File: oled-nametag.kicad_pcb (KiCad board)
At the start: 4 copper layers, 88 x 30 mm, 138 parts, among them J1 USB_C_Receptacle_USB2.0, J2 I2C, J3 LOAD, Q1 AO3401A, Q2 AO3401A, Q4 AO3400A, Q5 AO3400A, Q6 2N7002, SW1 Power, SW2 BTN1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

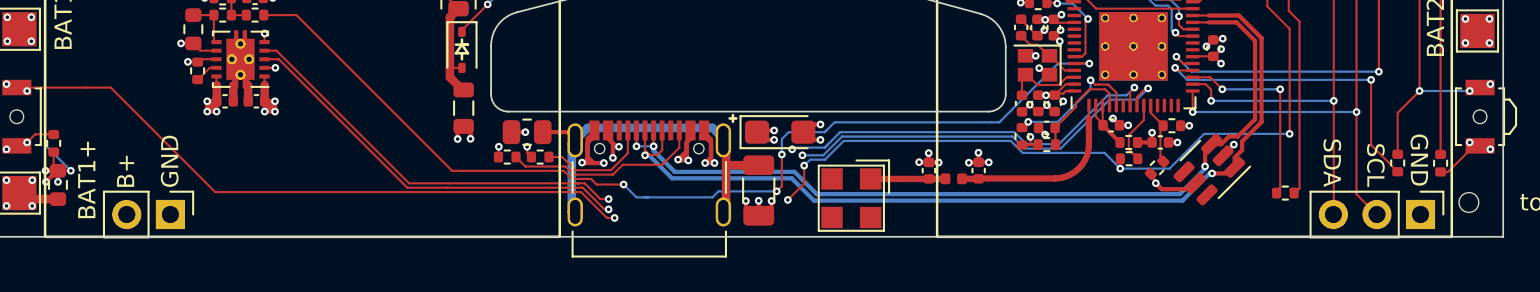
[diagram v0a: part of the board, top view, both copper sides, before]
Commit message: Unify text orientation
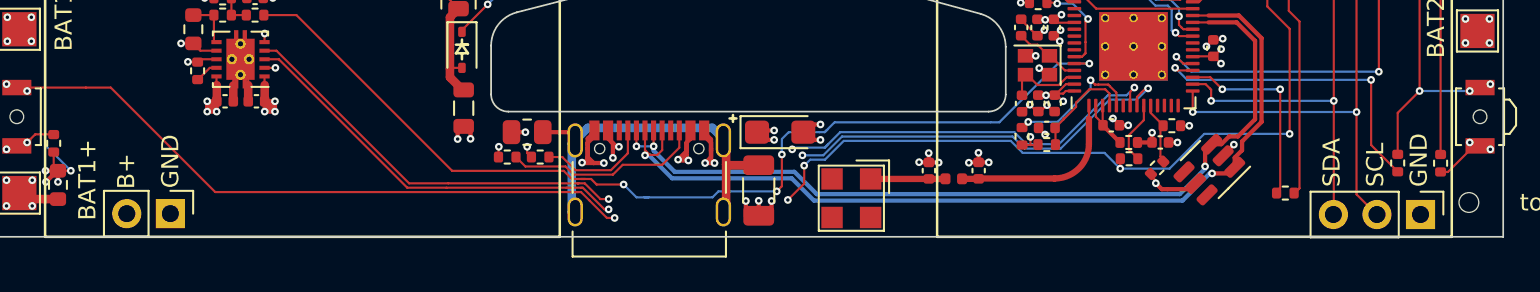
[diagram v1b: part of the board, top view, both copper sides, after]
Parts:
- moved J3 0.05 mm to (30.3, 48.6)
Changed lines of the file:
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@@
   )
   (footprint "Connector_PinHeader_2.54mm:PinHeader_1x02_P2.54mm_Vertical" (layer "F.Cu")
-    (at 30.3 48.7 -90)
+    (at 30.3 48.65 -90)
     (descr "Through hole straight pin header, 1x02, 2.54mm pitch, single row")
     (tags "Through hole pin header THT 1x02 2.54mm single row")
@@
     (effects (font (size 1 1) (thickness 0.15)) (justify left))
   )
-  (gr_text "GND" (at 103.079999 47.1 -90) (layer "F.SilkS")
-    (effects (font (size 1 1) (thickness 0.15)) (justify right))
+  (gr_text "GND" (at 103.079999 47.1 90) (layer "F.SilkS")
+    (effects (font (size 1 1) (thickness 0.15)) (justify left))
   )
-  (gr_text "SCL" (at 100.54 47.1 -90) (layer "F.SilkS")
-    (effects (font (size 1 1) (thickness 0.15)) (justify right))
+  (gr_text "SCL" (at 100.54 47.1 90) (layer "F.SilkS")
+    (effects (font (size 1 1) (thickness 0.15)) (justify left))
   )
   (gr_text "JLCJLCJLCJLC" (at 64 32.85) (layer "F.SilkS")
@@
     (effects (font (size 1 1) (thickness 0.15)) (justify left))
   )
-  (gr_text "SDA" (at 98 47.1 -90) (layer "F.SilkS")
-    (effects (font (size 1 1) (thickness 0.15)) (justify right))
+  (gr_text "SDA" (at 98 47.1 90) (layer "F.SilkS")
+    (effects (font (size 1 1) (thickness 0.15)) (justify left))
   )
   (gr_text "BAT1+" (at 24.88 46.68 90) (layer "F.SilkS")

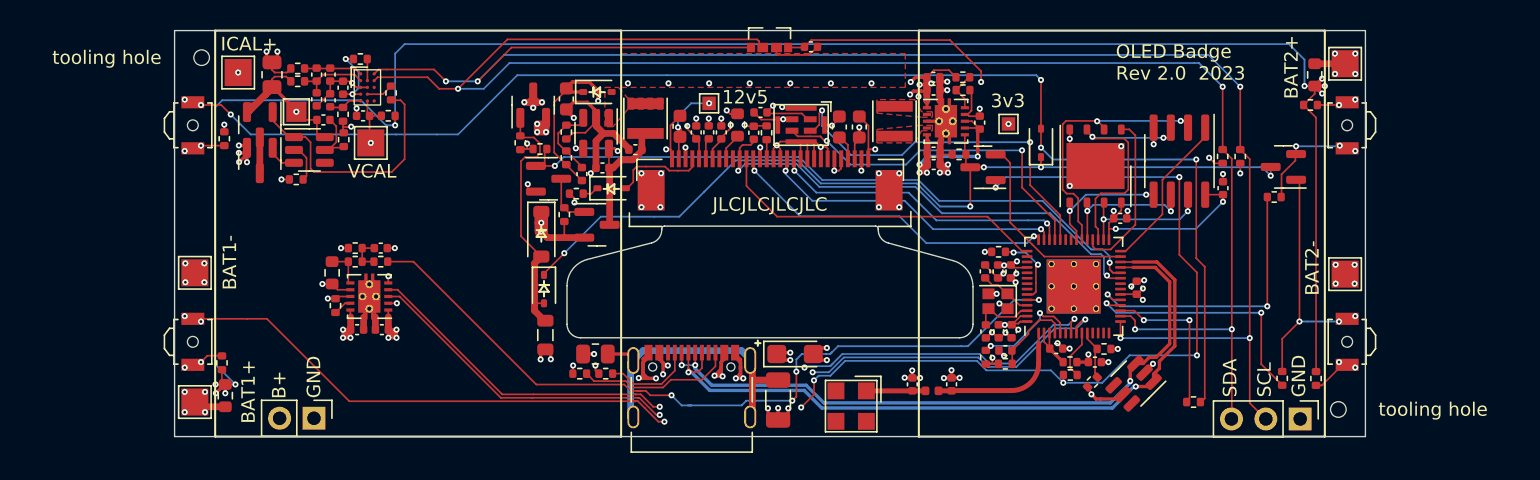
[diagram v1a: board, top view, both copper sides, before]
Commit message: Add thermal groundplane to charger
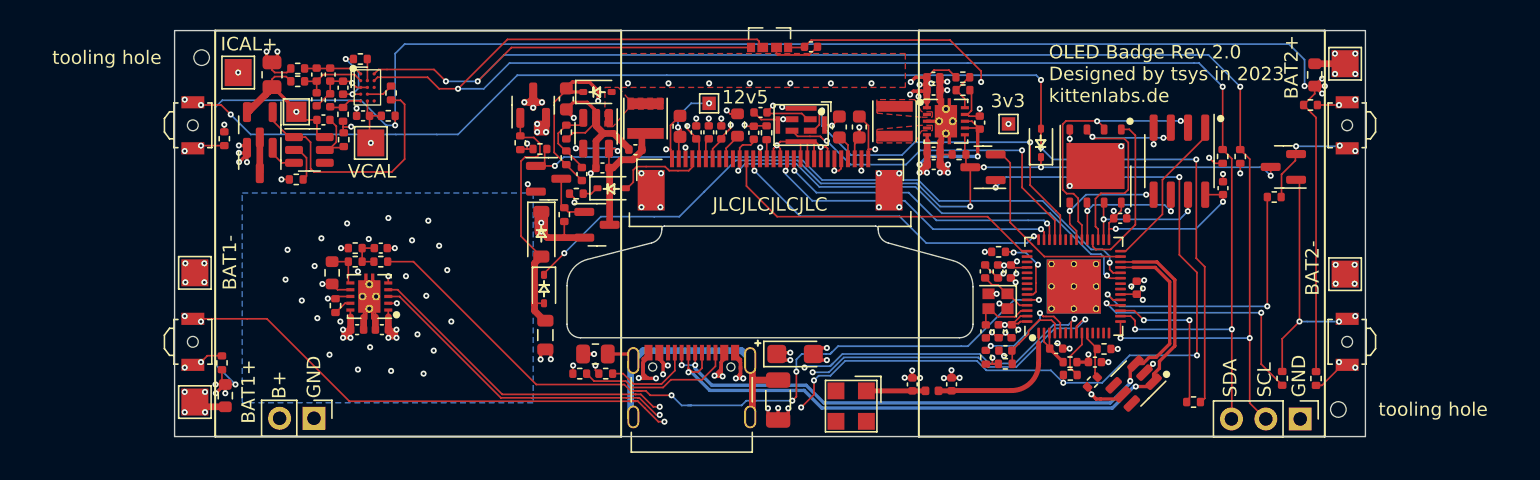
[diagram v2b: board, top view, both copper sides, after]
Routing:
- net GND: vias 93 -> 118
- added copper zone on B.Cu, net GND
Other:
- board text added: "OLED Badge Rev 2.0 Designed by tsys in 2023 kittenlabs.de"
- board text removed: "OLED Badge Rev 2.0 2023"

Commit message: Improve thermal via stitching on charger IC
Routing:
- net GND: vias 118 -> 122
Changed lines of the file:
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@@
   (segment (start 54.975 45.7) (end 54.425 45.7) (width 0.25) (layer "F.Cu") (net 6))
   (segment (start 51.15 26.75) (end 50.35 27.55) (width 0.127) (layer "F.Cu") (net 6))
+  (via (at 28.4 41.35) (size 0.45) (drill 0.2) (layers "F.Cu" "B.Cu") (free) (net 6))
   (via (at 68.75 30.35) (size 0.45) (drill 0.2) (layers "F.Cu" "B.Cu") (net 6))
   (via (at 59.5 23.9) (size 0.45) (drill 0.2) (layers "F.Cu" "B.Cu") (free) (net 6))
@@
   (via (at 58.55 26.5) (size 0.45) (drill 0.2) (layers "F.Cu" "B.Cu") (net 6))
   (via (at 24.75 29.0375) (size 0.45) (drill 0.2) (layers "F.Cu" "B.Cu") (net 6))
+  (via (at 29.2 34.45) (size 0.45) (drill 0.2) (layers "F.Cu" "B.Cu") (free) (net 6))
   (via (at 55.575 45.7) (size 0.45) (drill 0.2) (layers "F.Cu" "B.Cu") (net 6))
   (via (at 30.55 41.25) (size 0.45) (drill 0.2) (layers "F.Cu" "B.Cu") (free) (net 6))
@@
   (via (at 97.475 30.6) (size 0.45) (drill 0.2) (layers "F.Cu" "B.Cu") (net 6))
   (via (at 46.1 31.35) (size 0.45) (drill 0.2) (layers "F.Cu" "B.Cu") (net 6))
+  (via (at 26.9 39.9) (size 0.45) (drill 0.2) (layers "F.Cu" "B.Cu") (free) (net 6))
   (via (at 38.6 39.6) (size 0.45) (drill 0.2) (layers "F.Cu" "B.Cu") (free) (net 6))
   (via (at 72.05 30.55) (size 0.45) (drill 0.2) (layers "F.Cu" "B.Cu") (net 6))
@@
   (via (at 77.15 30.5) (size 0.45) (drill 0.2) (layers "F.Cu" "B.Cu") (net 6))
   (via (at 76.55 30.5) (size 0.45) (drill 0.2) (layers "F.Cu" "B.Cu") (net 6))
+  (via (at 29.7 43.45) (size 0.45) (drill 0.2) (layers "F.Cu" "B.Cu") (free) (net 6))
   (via (at 24.75 28.4875) (size 0.45) (drill 0.2) (layers "F.Cu" "B.Cu") (net 6))
   (via (at 55.95 30.55) (size 0.45) (drill 0.2) (layers "F.Cu" "B.Cu") (net 6))
